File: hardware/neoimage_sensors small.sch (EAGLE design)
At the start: 26 parts, among them U1 LIS3DH, U2 OPA344, U3 ICS-40300, U4 STM32F030F4P6TR, U5 TEMT6000

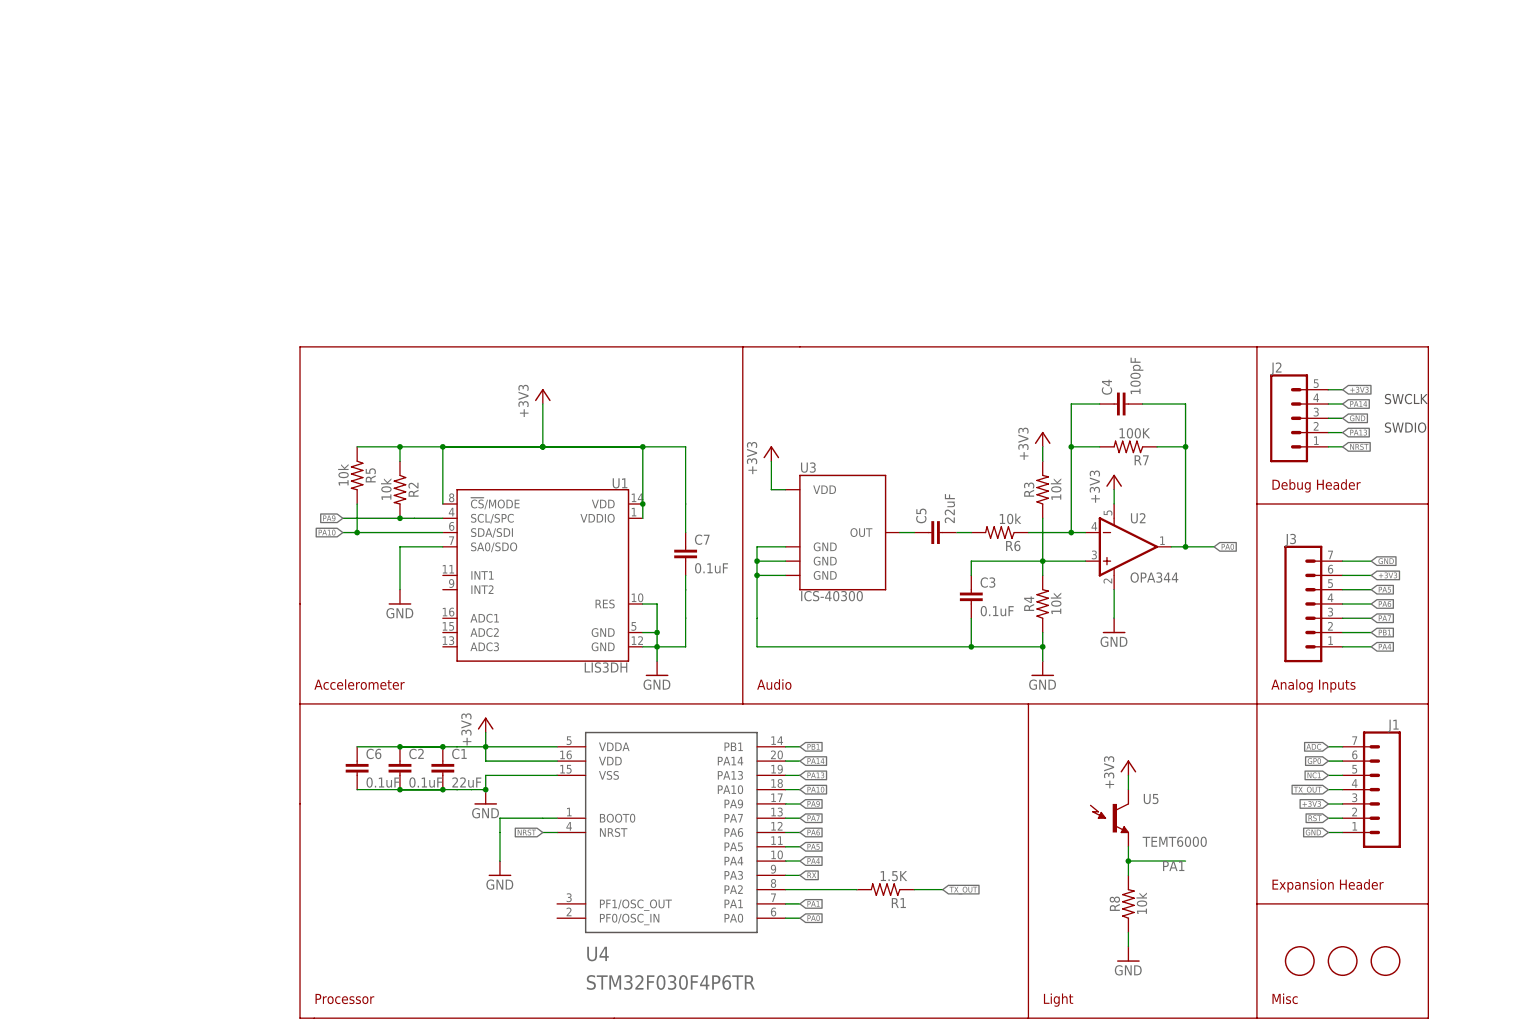
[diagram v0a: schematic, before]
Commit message: v1.8 of board
switch to 0603, fix analog, labels
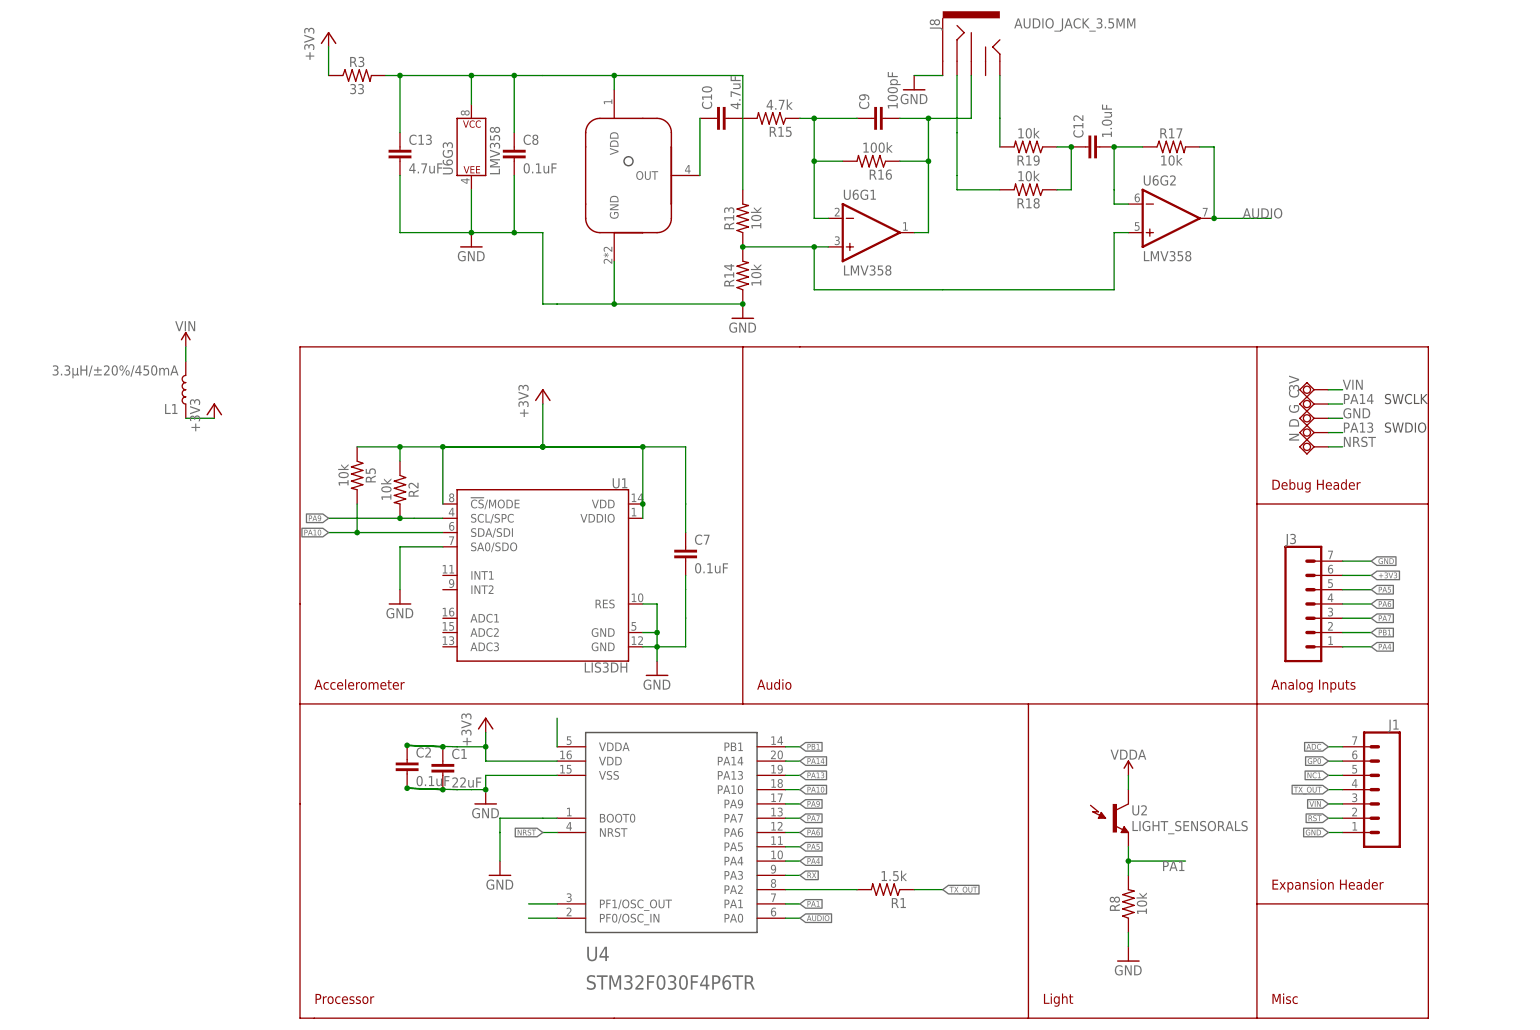
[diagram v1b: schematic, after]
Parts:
- removed C3, C6: 0.1uF, SparkFun-Capacitors:0.1UF-0402-16V-10%
- removed C4: 100pF, SparkFun:CAP0402-CAP
- removed C5: 22uF, SparkFun-Capacitors:22UF-0805-6.3V-20%
- removed FID1, FID2, FID3: FIDUCIAL, adafruit:FIDUCIAL
- removed J2: (no value), SparkFun-Connectors:CONN_05LOCK
- removed R4: 10k, SparkFun-Resistors:RESISTOR0402
- removed R6: 10k, SparkFun:RESISTOR0402-RES
- removed R7: 100K, SparkFun:RESISTOR0402-RES
- removed U3: ICS-40300, SparkFun:ADMP401
- removed U5: TEMT6000, SparkFun:TEMT6000
- added 3V, C, D, G, N: TPSQTP18SQ, testpad:TPSQTP18SQ
- added C10, C13: 4.7uF, SparkFun-Capacitors:4.7UF0603
- added C12: 1.0uF, SparkFun-Capacitors:1.0UF-0603-16V-10%
- added C8: 0.1uF, SparkFun-Capacitors:0.1UF-0603-25V-(+80/-20%)
- added C9: 100pF, SparkFun-Capacitors:100PF-0603-50V-5%
- added J8: AUDIO_JACK_3.5MM, SparkFun-Connectors:AUDIO_JACK_3.5MM_KIT
- added L1: 3.3µH/±20%/450mA, SparkFun-Coils:INDUCTOR-0805-3.3UH
- added R13, R14, R17, R18, R19: 10k, SparkFun-Resistors:10KOHM-0603-1/10W-1%
- added R15: 4.7k, SparkFun-Resistors:4.7KOHM-0603-1/10W-1%
- added R16: 100k, SparkFun-Resistors:100KOHM-0603-1/10W-1%
- added U$3: MICROPHONE-MEMS, bens:MICROPHONE-MEMS
- added U6: LMV358, SparkFun-IC-Amplifiers:LMV358SOIC
- C2, C7: device SparkFun-Capacitors:0.1UF-0402-16V-10% -> SparkFun-Capacitors:0.1UF-0603-25V-(+80/-20%)
- R1: value 1.5K -> 1.5k; device SparkFun:RESISTOR0402-RES -> SparkFun-Resistors:1.5KOHM-0603-1/10W-1%
- R2, R5, R8: device SparkFun-Resistors:RESISTOR0402 -> SparkFun-Resistors:10KOHM-0603-1/10W-1%
- R3: value 10k -> 33; device SparkFun-Resistors:RESISTOR0402 -> SparkFun-Resistors:33OHM-0603-1/10W-1%
- U2: value OPA344 -> LIGHT_SENSORALS; device SparkFun:OPA344 -> SparkFun-Sensors:LIGHT_SENSORALS
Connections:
- removed net N$3: C4.1, R6.1, R7.2, U2.-IN
- removed net N$6: C5.2, R6.2
- removed net N$7: C3.1, R3.1, R4.2, U2.+IN
- removed net PA0: C4.2, R7.1, U2.OUT, U4.PA0
- new net AUDIO: R17.2, U4.PA0, U6G2.OUT
- new net MICOUT: C9.2, J8.RSH, R16.1, U6G1.OUT
- new net N$1: U4.PF1/OSC_OUT
- new net N$21: C10.1, U$3.OUT
- new net N$22: C9.1, R15.1, R16.2, U6G1.-IN
- new net N$23: C10.2, R15.2
- new net N$24: R13.1, R14.2, U6G1.+IN, U6G2.+IN
- new net N$25: C12.1, R18.1, R19.1
- new net N$26: C12.2, R17.1, U6G2.-IN
- new net N$27: J8.TIP, R19.2
- new net N$28: J8.RING, R18.2
- new net VDDA: C13.1, C8.1, R13.2, R3.2, U$3.VDD, U2.C1, U4.VDDA, U6G3.P$V+
- new net VIN: 3V.TP, J1.3, L1.2
- net +3V3: now also L1.1, R3.1; no longer C6.1, J1.3, J2.5, R3.2, U2.V+, U3.VDD, U4.VDDA, U5.C1
- net GND: now also C13.2, C8.2, G.TP, J8.SLEEVE, R14.1, U$3.GND, U6G3.P$V-; no longer C3.2, C6.2, J2.3, R4.1, U2.V-, U3.GND@2, U3.GND@4, U3.GND@6
- net N$2: now also U4.PF0/OSC_IN; no longer C5.1, U3.OUT
- net NRST: now also N.TP; no longer J2.1
- net PA1: now also U2.E1; no longer U5.E1
- net PA13: now also D.TP; no longer J2.2
- net PA14: now also C.TP; no longer J2.4
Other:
- moved on the sheet: C2, R3

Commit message: cleanup schematic, name signals, pdf
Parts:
- L1: value 3.3µH/±20%/450mA -> 1µH
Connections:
- net PA1 renamed LIGHT
- net PA10 renamed SCL
- net PA13 renamed SWDIO
- net PA14 renamed SWCLK
- net PA4 renamed AIN0
- net PA5 renamed AIN4
- net PA6 renamed AIN3
- net PA7 renamed AIN2
- net PA9 renamed SDA
- net PB1 renamed AIN1
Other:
- note added: "Amp"
- note added: "Mic"
- note added: "Mixer/Buffer"
- note added: "Pixelblaze Sensor Expansion Board v1.8 2019 Ben Hencke electromage.com"
- note added: "Power Filtering"
- note removed: "Audio"
- note removed: "Misc"
- note removed: "SWCLK"
- note removed: "SWDIO"
- moved on the sheet: 3V, C, C1, C10, C12, C13, C2, C7, C8, C9, D, G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
